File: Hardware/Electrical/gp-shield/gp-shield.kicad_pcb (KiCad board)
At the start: 2 copper layers, 72.4 x 53.3 mm, 211 parts, among them J1 XT60/TERM2, J10 Conn_01x08, J11 Conn_01x04, J12 Conn_01x08, J13 T821-02x08, J14 Conn_01x04, J15 Conn_01x07, J2 XT60/TERM2, J3 Conn_01x04, J4 Conn_01x03, J5 Conn_01x03, J6 Conn_01x03, J7 Conn_01x03, J8 Conn_01x03, J9 Conn_01x03, Q1 Q_PMOS_GDS, Q3 Q_NMOS_GDS, SW1 SW_SPDT, SW2 SW_Push, SW3 SW_Push, U1 NCP1117-5.0_SOT223, U2 LM4040DBZ-2.5, U4 LM397

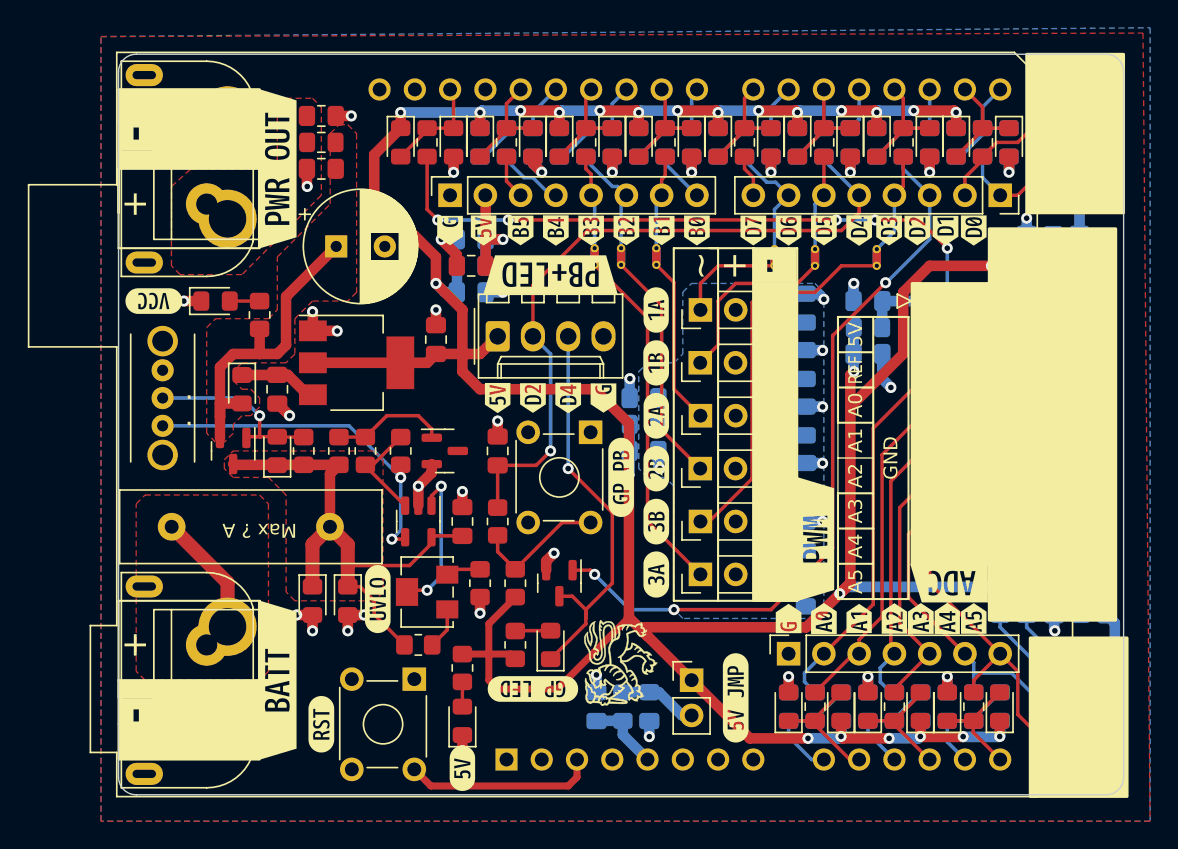
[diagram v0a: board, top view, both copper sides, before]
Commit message: Updated footprints and PCB layout
Updated reverse polarity and overvoltage to use bidirectional TVS diode
Changed footprint of TVS diode
Changed footprint of fuse to proper 5x20mm fuse holder
Changed footprint of PMOS high side switch to DPAK
Updated layout with Vreg on backside
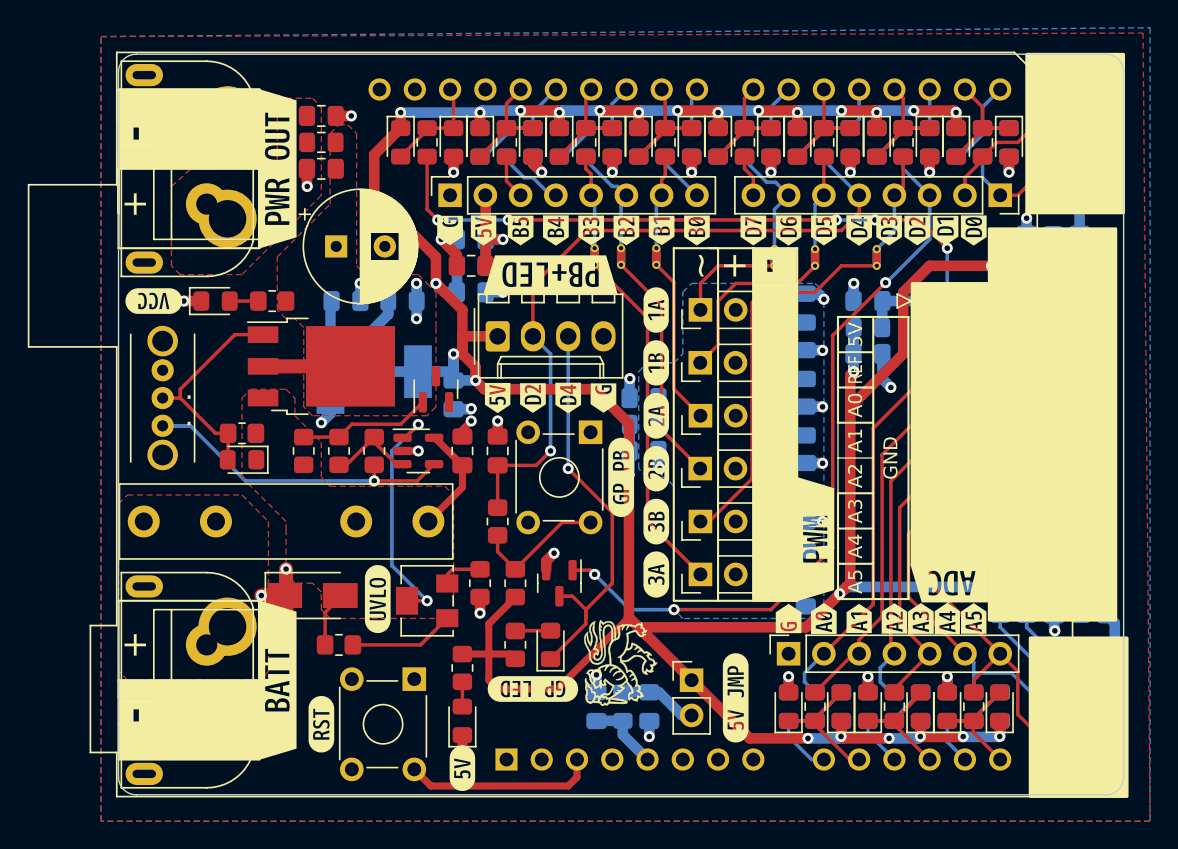
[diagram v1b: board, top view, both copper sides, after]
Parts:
- removed D3: 25V?, Diode_SMD:D_0805_2012Metric_Pad1.15x1.40mm_HandSolder
- C1, C2, D1, U1: moved to B.Cu
- D2: value D_Schottky -> D_TVS; footprint Diode_SMD:D_0805_2012Metric_Pad1.15x1.40mm_HandSolder -> Diode_SMD:D_SMA
- F1: footprint Fuse:Fuse_Littelfuse-LVR100 -> Fuse:Fuseholder_Littelfuse_445_030_series_5x20mm
- Q1: footprint Package_TO_SOT_SMD:SOT-23 -> Package_TO_SOT_SMD:TO-252-3_TabPin2
- moved D1 13.2 mm to (107.4, 69.2), turned to 0 degrees
- moved Q1 8.80 mm to (101.6, 73.9), turned to 0 degrees
- moved C1 8.05 mm to (103.4, 69.2), turned to 0 degrees
- moved R1 5.71 mm to (102.9, 94.0)
- moved C3 5.08 mm to (111.8, 80.0)
- moved U4 5.08 mm to (108.6, 80.0), turned to 0 degrees
- moved R10 4.62 mm to (95.9, 78.7), turned to 180 degrees
- moved U2 4.49 mm to (109.9, 75.6), turned to 90 degrees
- moved C2 4.18 mm to (111.1, 76.0), turned to -90 degrees
- moved D4 2.62 mm to (95.9, 80.6), turned to 180 degrees
- moved R3 2.54 mm to (100.3, 80.0)
- moved F1 2.05 mm to (88.8, 85.1)
- moved R4 1.91 mm to (102.9, 80.0)
- moved R9 1.91 mm to (105.4, 80.0)
- moved U1 1.42 mm to (105.4, 74.3)
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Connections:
- D2 pad 1: /Power/+BATT_FUSED -> GND
- D2 pad 2: GND -> /Power/+BATT_FUSED
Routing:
- net /Power/+BATT_FUSED: track 37.9 -> 12.0 mm
- net VCC: track 23.5 -> 9.23 mm, vias 0 -> 2
- net +BATT: track 8.87 -> 0.00 mm
- net /Power/VCC_CMP-: track 11.1 -> 18.0 mm
- net /Power/VCC_CMP_POT+: track 3.01 -> 7.60 mm
- net +5V: track 264.2 -> 268.0 mm, vias 25 -> 27
- net VCC_REG: track 5.70 -> 8.74 mm
- net /Power/VCC_EN: track 13.2 -> 15.9 mm, vias 1 -> 0
- net GND: track 72.1 -> 70.0 mm, vias 46 -> 44
- net /Power/VCC_VREF: track 8.34 -> 9.61 mm
- net /Power/VCC_CMP+: track 7.50 -> 6.43 mm
- net /Power/VCC_CMP_OUT: track 25.3 -> 24.7 mm, vias 2 -> 1
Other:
- board text added: "6V->24V"
- board text added: "gp-shield Rev. A"
- board text removed: "6V->20V"
- board text removed: "Max ? A"
- board text removed: "gp-shield Rev. A A Marshall 2022"
